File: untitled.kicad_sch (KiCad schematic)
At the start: 25 parts, among them U1 RP2040, X1 ASE-12.0MHz

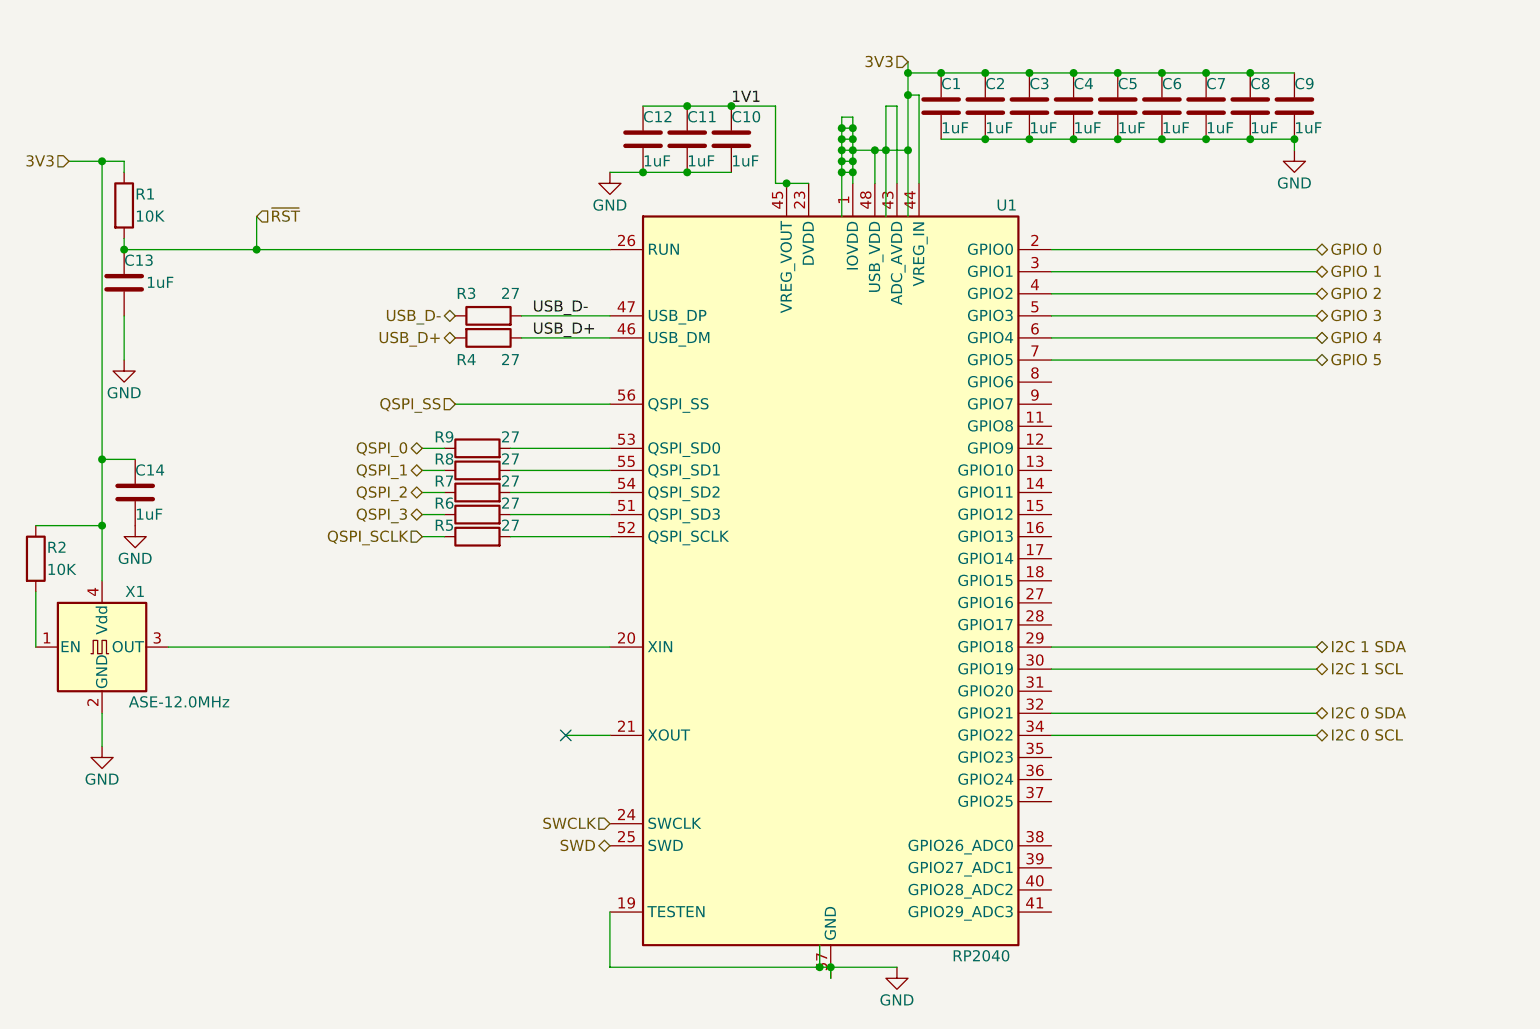
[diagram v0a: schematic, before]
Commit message: adds 2 new PWM PINS for the Motors
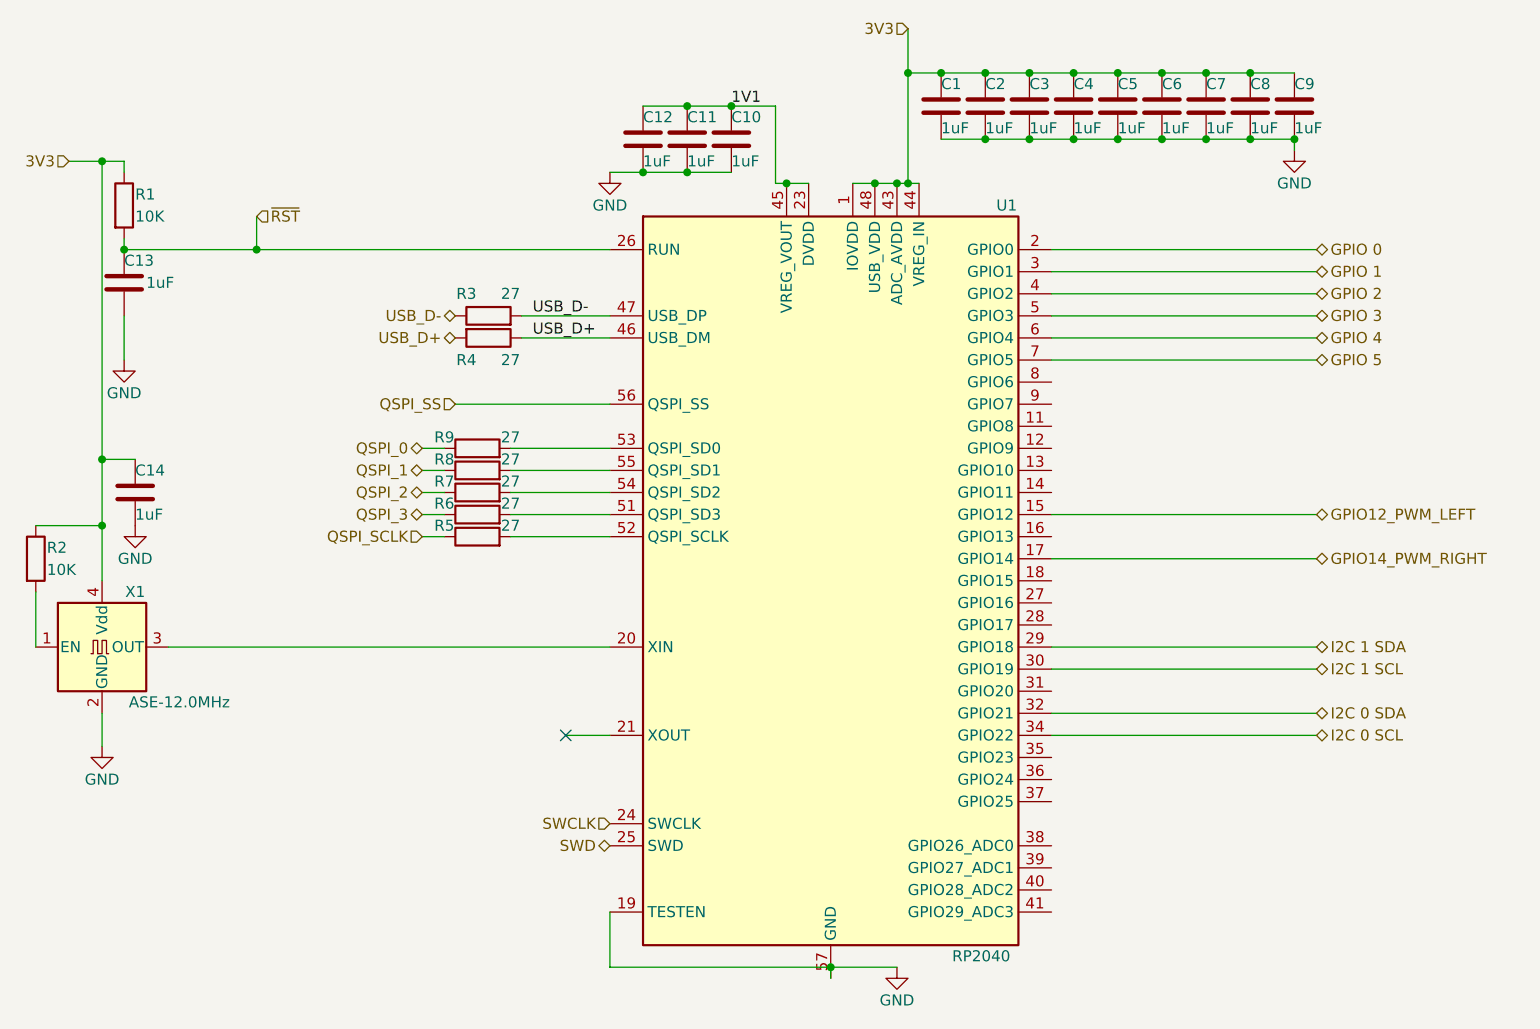
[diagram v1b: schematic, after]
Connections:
- net GPIO12_PWM_LEFT: now reaches U1.15 (GPIO12)
- net GPIO14_PWM_RIGHT: now reaches U1.17 (GPIO14)

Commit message: started PCB layout
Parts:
- C1, C10, C11, C12, C13, C14, C2, C3, C4, C5, C6, C7, C8, C9: footprint (none) -> Capacitor_SMD:C_0201_0603Metric
- R1, R2, R3, R4, R5, R6, R7, R8, R9: footprint (none) -> Resistor_SMD:R_0201_0603Metric
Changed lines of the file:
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@@
       (effects (font (size 1.27 1.27)))
     )
-    (property "Footprint" "" (at 77.47 76.708 90)
+    (property "Footprint" "Resistor_SMD:R_0201_0603Metric" (at 77.47 76.708 90)
       (effects (font (size 1.27 1.27)) hide)
     )
@@
       (effects (font (size 1.27 1.27)) (justify left))
     )
-    (property "Footprint" "" (at 107.6452 33.02 0)
+    (property "Footprint" "Capacitor_SMD:C_0201_0603Metric" (at 107.6452 33.02 0)
       (effects (font (size 1.27 1.27)) hide)
     )
@@
       (effects (font (size 1.27 1.27)) (justify left))
     )
-    (property "Footprint" "" (at 24.892 77.47 90)
+    (property "Footprint" "Resistor_SMD:R_0201_0603Metric" (at 24.892 77.47 90)
       (effects (font (size 1.27 1.27)) hide)
     )
@@
       (effects (font (size 1.27 1.27)))
     )
-    (property "Footprint" "" (at 77.47 66.548 90)
+    (property "Footprint" "Resistor_SMD:R_0201_0603Metric" (at 77.47 66.548 90)
       (effects (font (size 1.27 1.27)) hide)
     )
@@
       (effects (font (size 1.27 1.27)) (justify left))
     )
-    (property "Footprint" "" (at 136.8552 29.21 0)
+    (property "Footprint" "Capacitor_SMD:C_0201_0603Metric" (at 136.8552 29.21 0)
       (effects (font (size 1.27 1.27)) hide)
     )
@@
       (effects (font (size 1.27 1.27)) (justify left))
     )
-    (property "Footprint" "" (at 157.1752 29.21 0)
+    (property "Footprint" "Capacitor_SMD:C_0201_0603Metric" (at 157.1752 29.21 0)
       (effects (font (size 1.27 1.27)) hide)
     )
@@
       (effects (font (size 1.27 1.27)))
     )
-    (property "Footprint" "" (at 77.47 74.168 90)
+    (property "Footprint" "Resistor_SMD:R_0201_0603Metric" (at 77.47 74.168 90)
       (effects (font (size 1.27 1.27)) hide)
     )
@@
       (effects (font (size 1.27 1.27)) (justify left))
     )
-    (property "Footprint" "" (at 147.0152 29.21 0)
+    (property "Footprint" "Capacitor_SMD:C_0201_0603Metric" (at 147.0152 29.21 0)
       (effects (font (size 1.27 1.27)) hide)
     )
@@
       (effects (font (size 1.27 1.27)) (justify left))
     )
-    (property "Footprint" "" (at 152.0952 29.21 0)
+    (property "Footprint" "Capacitor_SMD:C_0201_0603Metric" (at 152.0952 29.21 0)
       (effects (font (size 1.27 1.27)) hide)
     )
@@
       (effects (font (size 1.27 1.27)) (justify left))
     )
-    (property "Footprint" "" (at 162.2552 29.21 0)
+    (property "Footprint" "Capacitor_SMD:C_0201_0603Metric" (at 162.2552 29.21 0)
       (effects (font (size 1.27 1.27)) hide)
     )
@@
       (effects (font (size 1.27 1.27)) (justify left))
     )
-    (property "Footprint" "" (at 39.0652 73.66 0)
+    (property "Footprint" "Capacitor_SMD:C_0201_0603Metric" (at 39.0652 73.66 0)
       (effects (font (size 1.27 1.27)) hide)
     )
@@
       (effects (font (size 1.27 1.27)))
     )
-    (property "Footprint" "" (at 77.47 71.628 90)
+    (property "Footprint" "Resistor_SMD:R_0201_0603Metric" (at 77.47 71.628 90)
       (effects (font (size 1.27 1.27)) hide)
     )
@@
       (effects (font (size 1.27 1.27)) (justify left))
     )
-    (property "Footprint" "" (at 172.4152 29.21 0)
+    (property "Footprint" "Capacitor_SMD:C_0201_0603Metric" (at 172.4152 29.21 0)
       (effects (font (size 1.27 1.27)) hide)
     )
@@
       (effects (font (size 1.27 1.27)) (justify left))
     )
-    (property "Footprint" "" (at 131.7752 29.21 0)
+    (property "Footprint" "Capacitor_SMD:C_0201_0603Metric" (at 131.7752 29.21 0)
       (effects (font (size 1.27 1.27)) hide)
     )
@@
       (effects (font (size 1.27 1.27)))
     )
-    (property "Footprint" "" (at 78.74 51.308 90)
+    (property "Footprint" "Resistor_SMD:R_0201_0603Metric" (at 78.74 51.308 90)
       (effects (font (size 1.27 1.27)) hide)
     )
@@
       (effects (font (size 1.27 1.27)))
     )
-    (property "Footprint" "" (at 78.74 50.292 90)
+    (property "Footprint" "Resistor_SMD:R_0201_0603Metric" (at 78.74 50.292 90)
       (effects (font (size 1.27 1.27)) hide)
     )
@@
       (effects (font (size 1.27 1.27)))
     )
-    (property "Footprint" "" (at 77.47 69.088 90)
+    (property "Footprint" "Resistor_SMD:R_0201_0603Metric" (at 77.47 69.088 90)
       (effects (font (size 1.27 1.27)) hide)
     )
@@
       (effects (font (size 1.27 1.27)) (justify left))
     )
-    (property "Footprint" "" (at 167.3352 29.21 0)
+    (property "Footprint" "Capacitor_SMD:C_0201_0603Metric" (at 167.3352 29.21 0)
       (effects (font (size 1.27 1.27)) hide)
     )
@@
       (effects (font (size 1.27 1.27)) (justify left))
     )
-    (property "Footprint" "" (at 37.7952 49.53 0)
+    (property "Footprint" "Capacitor_SMD:C_0201_0603Metric" (at 37.7952 49.53 0)
       (effects (font (size 1.27 1.27)) hide)
     )
@@
       (effects (font (size 1.27 1.27)) (justify left))
     )
-    (property "Footprint" "" (at 35.052 36.83 90)
+    (property "Footprint" "Resistor_SMD:R_0201_0603Metric" (at 35.052 36.83 90)
       (effects (font (size 1.27 1.27)) hide)
     )
@@
       (effects (font (size 1.27 1.27)) (justify left))
     )
-    (property "Footprint" "" (at 97.4852 33.02 0)
+    (property "Footprint" "Capacitor_SMD:C_0201_0603Metric" (at 97.4852 33.02 0)
       (effects (font (size 1.27 1.27)) hide)
     )
@@
       (effects (font (size 1.27 1.27)) (justify left))
     )
-    (property "Footprint" "" (at 102.5652 33.02 0)
+    (property "Footprint" "Capacitor_SMD:C_0201_0603Metric" (at 102.5652 33.02 0)
       (effects (font (size 1.27 1.27)) hide)
     )
@@
       (effects (font (size 1.27 1.27)) (justify left))
     )
-    (property "Footprint" "" (at 141.9352 29.21 0)
-      (effects (font (size 1.27 1.27)) hide)
-    )
+    (property "Footprint" "Capacitor_SMD:C_0201_0603Metric" (at 141.9352 29.21 0)
+      (effects (font (size 1.27 1.27)) hide)
+    )
